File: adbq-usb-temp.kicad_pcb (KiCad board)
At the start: 4 copper layers, 40.3 x 16 mm, 81 parts, among them J4 USB_C_Receptacle_USB2.0_14P, Q1 Q_NMOS, Q2 Q_NMOS, Q3 Q_NMOS, SW1 SW_Push, SW2 TestPoint, SW3 TestPoint, SW4 TestPoint, U1 ESP32-S3FH4R2, U14 TMP117AIDRV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

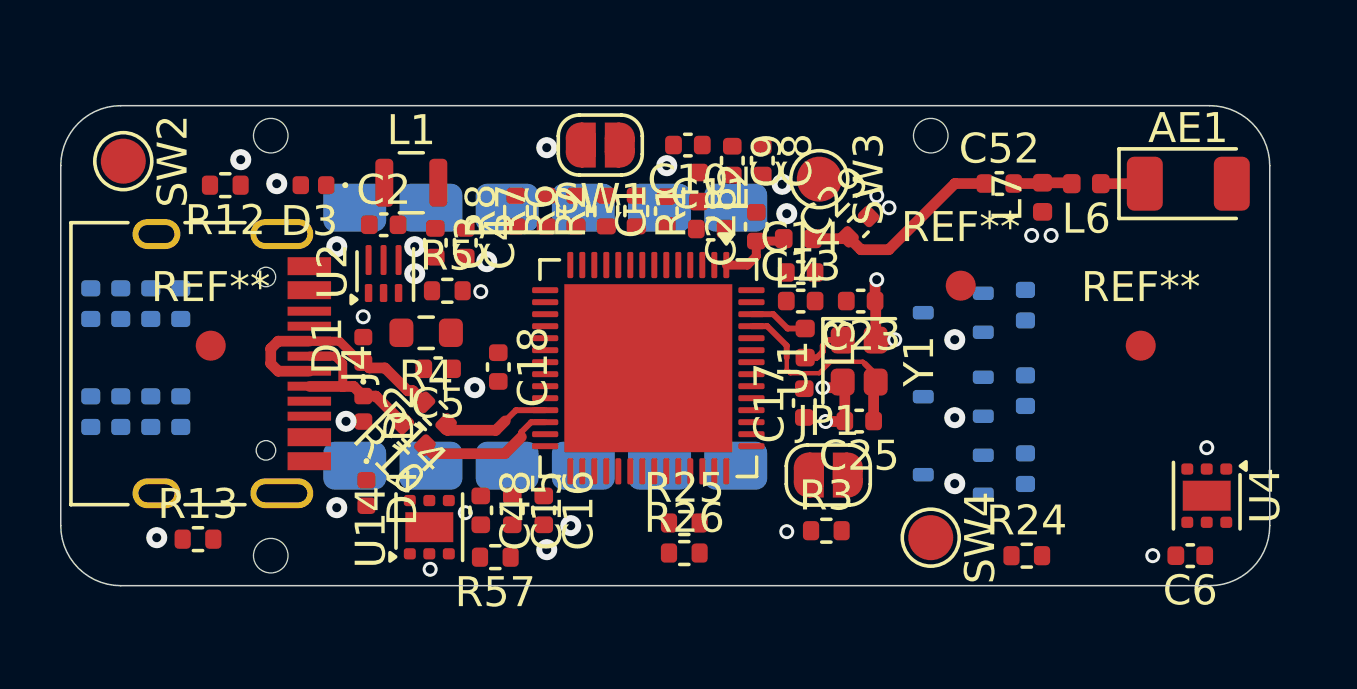
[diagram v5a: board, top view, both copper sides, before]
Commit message: pcb: add SMPS routing
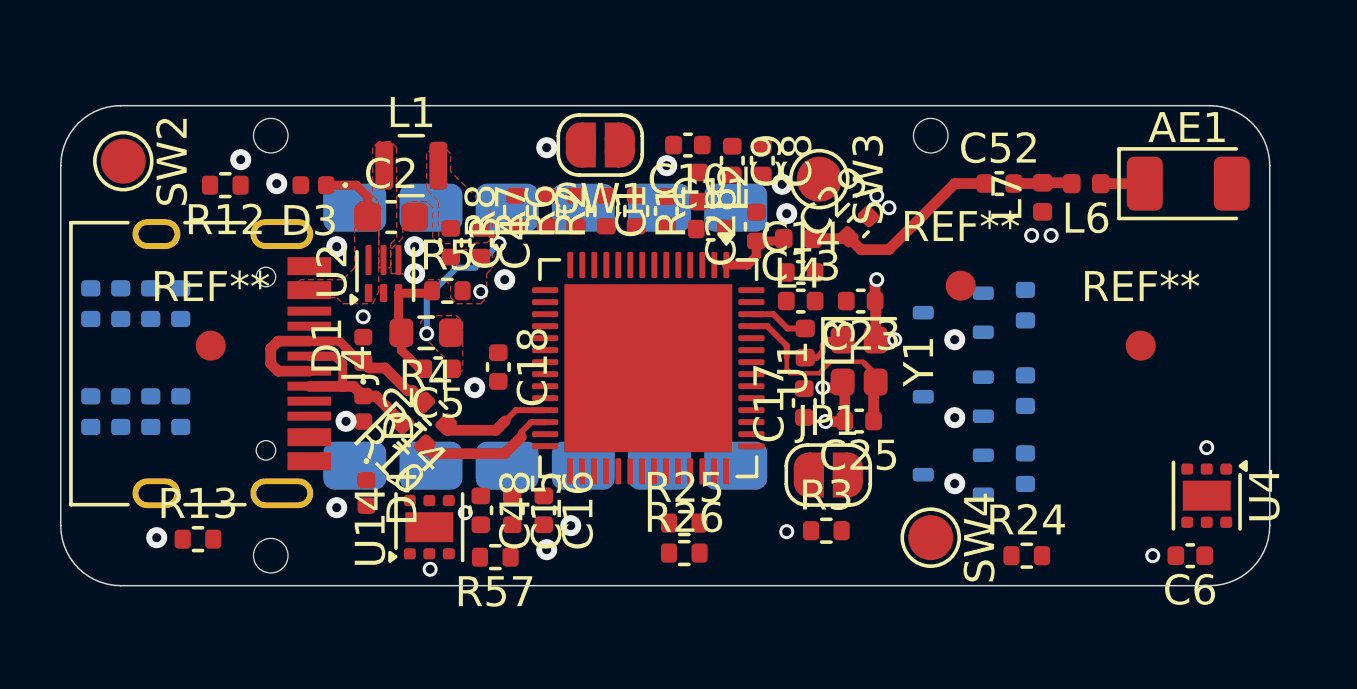
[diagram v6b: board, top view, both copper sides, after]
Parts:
- C2: footprint Capacitor_SMD:C_0402_1005Metric -> Capacitor_SMD:C_0603_1608Metric
- moved L1 0.57 mm to (93.7, 89.0)
- moved C3 0.52 mm to (95.0, 91.6)
- moved C4 0.52 mm to (96.0, 91.6)
- moved C2 0.36 mm to (93.0, 90.7)
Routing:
- net +3V3: track 0.00 -> 5.22 mm, vias 0 -> 2
- net Net-(U2-FB): track 0.00 -> 4.10 mm
- net +5V: track 0.00 -> 2.22 mm
- added copper zone on F.Cu, net +3V3
- added copper zone on F.Cu, net +5V
- added copper zone on F.Cu, net GND
- added copper zone on F.Cu, net Net-(U2-SW)

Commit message: pcb: add GPIO46 strapping routing
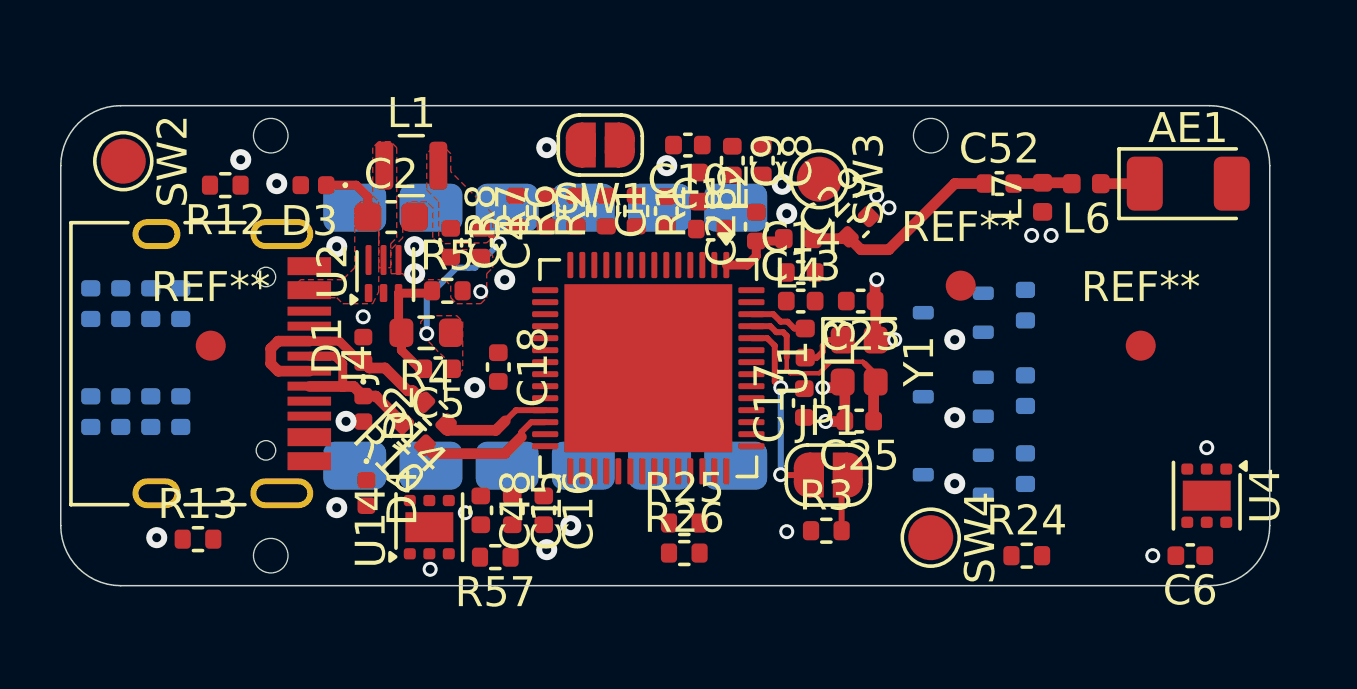
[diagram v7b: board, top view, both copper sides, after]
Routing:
- net Net-(JP1-A): track 0.00 -> 6.21 mm, vias 0 -> 2
- net Net-(JP1-B): track 0.00 -> 1.94 mm
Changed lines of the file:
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@@
+	)
+	(segment
+		(start 105.653611 94.35)
+		(end 105.0225 94.35)
+		(width 0.2)
+		(layer "F.Cu")
+		(net 10)
 	)
 	(segment
@@
 	)
 	(segment
-		(start 105.55 94.35)
-		(end 105.0225 94.35)
-		(width 0.2)
-		(layer "F.Cu")
-		(net 10)
-	)
-	(segment
 		(start 109.095 97.5125)
 		(end 109.095 96.2825)
 		(width 0.359)
-		(layer "F.Cu")
-		(net 10)
-	)
-	(segment
-		(start 106.2 95)
-		(end 105.55 94.35)
-		(width 0.2)
 		(layer "F.Cu")
 		(net 10)
@@
 	)
 	(segment
+		(start 106.082112 94.551)
+		(end 105.854612 94.551)
+		(width 0.2)
+		(layer "F.Cu")
+		(net 10)
+	)
+	(segment
 		(start 109.165 95.965)
 		(end 108.8 95.6)
@@
 	)
 	(segment
+		(start 106.2 94.668889)
+		(end 106.082112 94.551)
+		(width 0.2)
+		(layer "F.Cu")
+		(net 10)
+	)
+	(segment
 		(start 106.2 95.4)
-		(end 106.2 95)
+		(end 106.2 94.668889)
 		(width 0.2)
 		(layer "F.Cu")
@@
 	)
 	(segment
+		(start 105.854612 94.551)
+		(end 105.653611 94.35)
+		(width 0.2)
+		(layer "F.Cu")
+		(net 10)
+	)
+	(segment
 		(start 108.7365 95.5365)
 		(end 108.8 95.6)
@@
 	)
 	(segment
-		(start 105.75 93.95)
-		(end 106.2275 94.4275)
-		(width 0.2)
-		(layer "F.Cu")
-		(net 21)
-	)
-	(segment
-		(start 106.2275 94.4275)
+		(start 106.099862 99.299862)
+		(end 106.1125 99.3125)
+		(width 0.2)
+		(layer "F.Cu")
+		(net 18)
+	)
+	(segment
+		(start 105.8 95)
+		(end 105.8 96.2)
+		(width 0.2)
+		(layer "F.Cu")
+		(net 18)
+	)
+	(segment
+		(start 105.996113 99.299862)
+		(end 106.099862 99.299862)
+		(width 0.2)
+		(layer "F.Cu")
+		(net 18)
+	)
+	(segment
+		(start 106.1125 99.3125)
+		(end 106.935 99.3125)
+		(width 0.2)
+		(layer "F.Cu")
+		(net 18)
+	)
+	(segment
+		(start 105.8 96.2)
+		(end 106 96.4)
+		(width 0.2)
+		(layer "F.Cu")
+		(net 18)
+	)
+	(segment
+		(start 105.0225 94.75)
+		(end 105.55 94.75)
+		(width 0.2)
+		(layer "F.Cu")
+		(net 18)
+	)
+	(segment
+		(start 105.55 94.75)
+		(end 105.8 95)
+		(width 0.2)
+		(layer "F.Cu")
+		(net 18)
+	)
+	(via
+		(at 106 96.4)
+		(size 0.5)
+		(drill 0.3)
+		(layers "F.Cu" "B.Cu")
+		(net 18)
+	)
+	(via
+		(at 105.996113 99.299862)
+		(size 0.5)
+		(drill 0.3)
+		(layers "F.Cu" "B.Cu")
+		(net 18)
+	)
+	(segment
+		(start 106 99.2)
+		(end 106 96.4)
+		(width 0.2)
+		(layer "B.Cu")
+		(net 18)
+	)
+	(segment
+		(start 105.996113 99.203887)
+		(end 106 99.2)
+		(width 0.2)
+		(layer "B.Cu")
+		(net 18)
+	)
+	(segment
+		(start 105.996113 99.299862)
+		(end 105.996113 99.203887)
+		(width 0.2)
+		(layer "B.Cu")
+		(net 18)
+	)
+	(segment
+		(start 108.03 101.1675)
+		(end 108.03 99.5175)
+		(width 0.2)
+		(layer "F.Cu")
+		(net 19)
+	)
+	(segment
+		(start 108.03 99.5175)
+		(end 108.235 99.3125)
+		(width 0.2)
+		(layer "F.Cu")
+		(net 19)
+	)
+	(segment
+		(start 106.455 94.4275)
 		(end 106.815 94.4275)
 		(width 0.2)
@@
 		(width 0.2)
 		(layer "F.Cu")
+		(net 21)
+	)
+	(segment
+		(start 106 94.2)
+		(end 106.2275 94.2)
+		(width 0.2)
+		(layer "F.Cu")
+		(net 21)
+	)
+	(segment
+		(start 106.2275 94.2)
+		(end 106.455 94.4275)
+		(width 0.2)
+		(layer "F.Cu")
+		(net 21)
+	)
+	(segment
+		(start 105.75 93.95)
+		(end 106 94.2)
+		(width 0.2)
+		(layer "F.Cu")

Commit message: pcb: add i2c routing
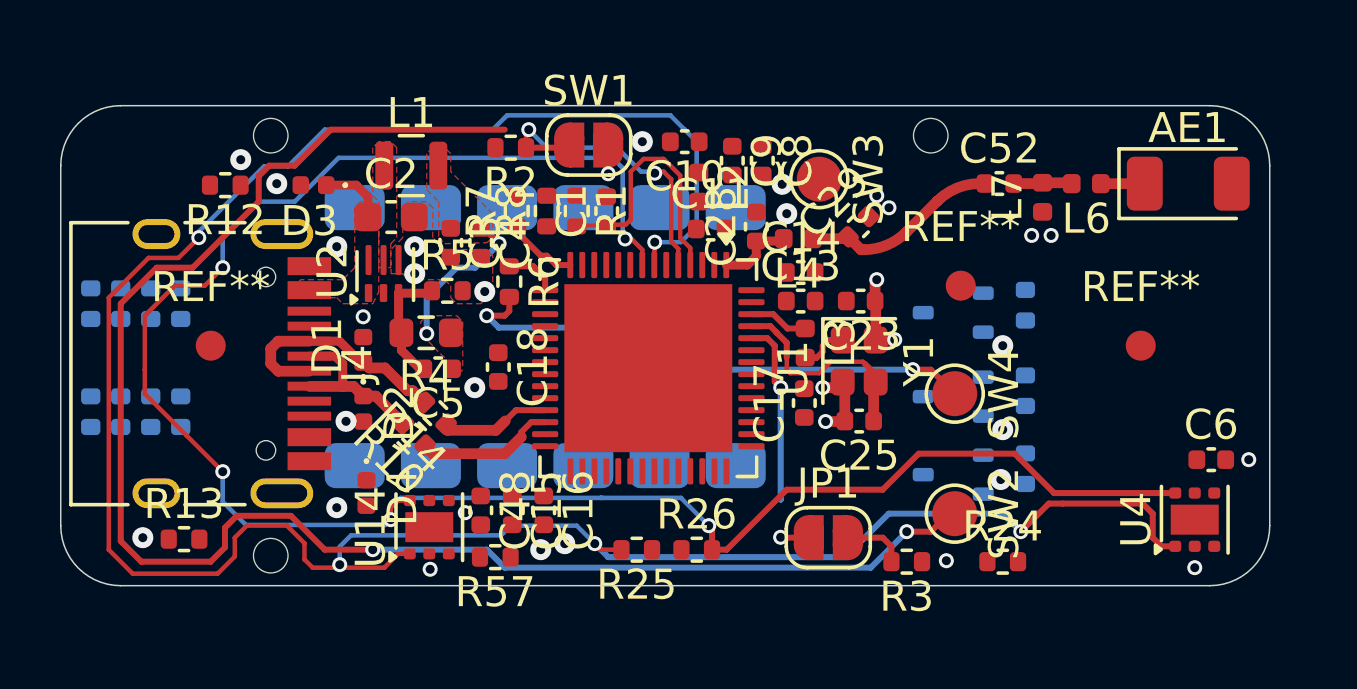
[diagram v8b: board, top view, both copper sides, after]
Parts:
- moved SW2 30.1 mm to (111.8, 100.6)
- moved SW4 4.87 mm to (111.8, 96.6)
- moved R2 3.82 mm to (97.0, 88.4), turned to 180 degrees
- moved C6 3.28 mm to (120.3, 98.8), turned to 0 degrees
- moved R6 3.24 mm to (97.0, 92.9), turned to -90 degrees
- moved R3 2.87 mm to (110.2, 102.2), turned to 180 degrees
- moved JP1 2.09 mm to (107.6, 101.4)
- moved C1 1.98 mm to (100.2, 90.5)
- moved R1 1.98 mm to (99.2, 90.5)
- moved R25 1.82 mm to (101.2, 101.8), turned to 180 degrees
- moved R8 1.03 mm to (98.2, 90.5)
- moved R7 0.98 mm to (97.2, 90.5)
- moved U4 0.89 mm to (119.8, 100.8), turned to 90 degrees
- moved R24 0.82 mm to (113.4, 102.2)
- moved R13 0.47 mm to (86.1, 101.5)
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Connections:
- R6 pad 1: Net-(U1-GPIO6/ADC1_CH5) -> Net-(U1-GPIO10/ADC1_CH9)
- R7 pad 1: Net-(U1-GPIO7/ADC1_CH6) -> Net-(U1-GPIO9/ADC1_CH8)
- U1 pad 11: Net-(U1-GPIO6/ADC1_CH5) -> unconnected-(U1-GPIO6/ADC1_CH5-Pad11)
- U1 pad 12: Net-(U1-GPIO7/ADC1_CH6) -> unconnected-(U1-GPIO7/ADC1_CH6-Pad12)
- U1 pad 14: unconnected-(U1-GPIO9/ADC1_CH8-Pad14) -> Net-(U1-GPIO9/ADC1_CH8)
- U1 pad 15: unconnected-(U1-GPIO10/ADC1_CH9-Pad15) -> Net-(U1-GPIO10/ADC1_CH9)
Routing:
- net /SCL: track 0.00 -> 81.3 mm, vias 0 -> 5
- net /SDA: track 0.00 -> 66.6 mm, vias 0 -> 5
- net Net-(R8-Pad2): track 0.00 -> 54.2 mm, vias 0 -> 2
- net Net-(R6-Pad2): track 0.00 -> 18.0 mm, vias 0 -> 2
- net /BOOT: track 0.00 -> 10.5 mm, vias 0 -> 2
- net Net-(U1-CHIP_PU/RESET): track 0.00 -> 8.67 mm
- net Net-(U1-GPIO9/ADC1_CH8): track 0.00 -> 2.34 mm
- net Net-(U1-GPIO10/ADC1_CH9): track 0.00 -> 1.76 mm
- net Net-(JP1-A): track 6.21 -> 6.92 mm
- net GND: vias 34 -> 33
